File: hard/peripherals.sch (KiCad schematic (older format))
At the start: 12 parts, among them J3 PJ-3062-CO, U1 ADXL362BCCZ-RLX, U2 ADXL345BCCZ-RL7

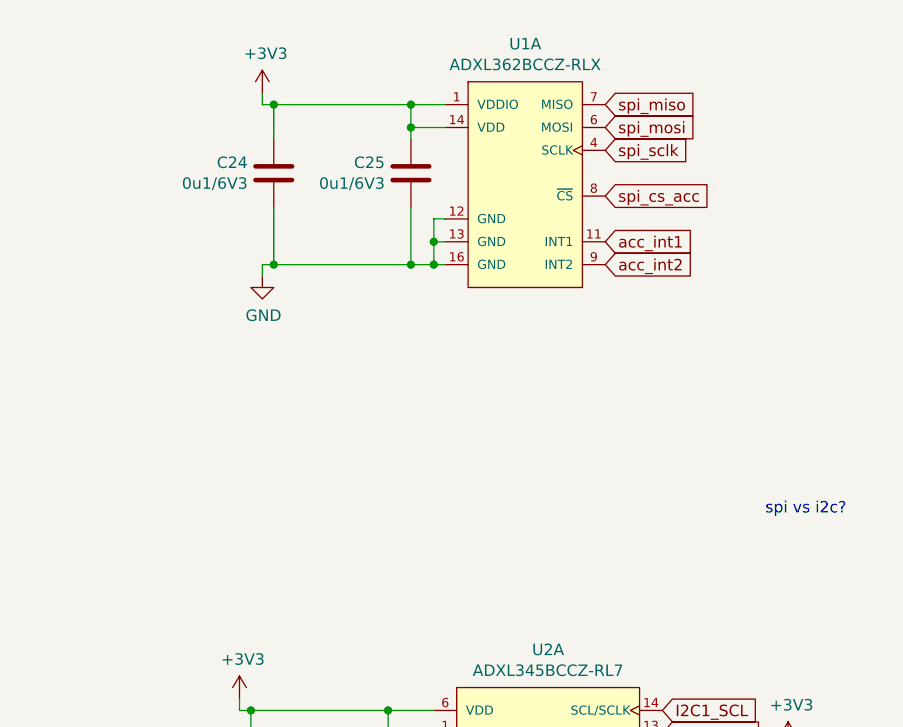
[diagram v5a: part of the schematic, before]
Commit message: general layout update
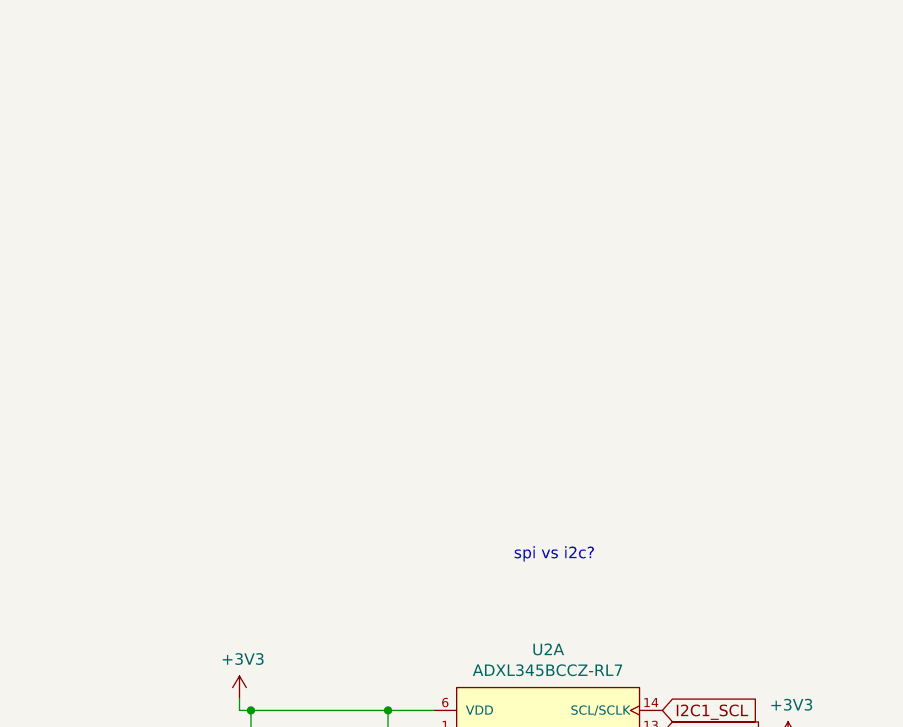
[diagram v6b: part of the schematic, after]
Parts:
- removed C24, C25: 0u1/6V3, Capacitor_SMD:C_0402_1005Metric, symbol Device:C
- removed U1: ADXL362BCCZ-RLX, led_matrix:Sensors_AnalogDevices_ADXL362BCCZ-RX, symbol led_matrix:ADXL362BCCZ-RLX
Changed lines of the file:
@@
 $EndDescr
-$Comp
-L Device:C C25
-U 1 1 613EB9FD
-P 8300 2150
-F 0 "C25" H 8186 2104 50  0000 R CNN
-F 1 "0u1/6V3" H 8186 2195 50  0000 R CNN
-F 2 "Capacitor_SMD:C_0402_1005Metric" H 8338 2000 50  0001 C CNN
-F 3 "~" H 8300 2150 50  0001 C CNN
-	1    8300 2150
-	1    0    0    1
-$EndComp
-$Comp
-L Device:C C24
-U 1 1 613EE98F
-P 7700 2150
-F 0 "C24" H 7586 2104 50  0000 R CNN
-F 1 "0u1/6V3" H 7586 2195 50  0000 R CNN
-F 2 "Capacitor_SMD:C_0402_1005Metric" H 7738 2000 50  0001 C CNN
-F 3 "~" H 7700 2150 50  0001 C CNN
-	1    7700 2150
-	1    0    0    1
-$EndComp
-$Comp
-L power:+3V3 #PWR0200
-U 1 1 613EF1A2
-P 7650 1800
-F 0 "#PWR0200" H 7650 1650 50  0001 C CNN
-F 1 "+3V3" H 7665 1973 50  0000 C CNN
-F 2 "" H 7650 1800 50  0001 C CNN
-F 3 "" H 7650 1800 50  0001 C CNN
-	1    7650 1800
-	1    0    0    -1
-$EndComp
-$Comp
-L power:GND #PWR0201
-U 1 1 613F21F8
-P 7650 2600
-F 0 "#PWR0201" H 7650 2350 50  0001 C CNN
-F 1 "GND" H 7655 2427 50  0000 C CNN
-F 2 "" H 7650 2600 50  0001 C CNN
-F 3 "" H 7650 2600 50  0001 C CNN
-	1    7650 2600
-	1    0    0    -1
-$EndComp
-Wire Wire Line
-	8450 2550 8400 2550
-Wire Wire Line
-	7650 2550 7650 2600
-Wire Wire Line
-	7700 2300 7700 2550
-Connection ~ 7700 2550
-Wire Wire Line
-	7700 2550 7650 2550
-Wire Wire Line
-	8300 2300 8300 2550
-Connection ~ 8300 2550
-Wire Wire Line
-	8300 2550 7700 2550
-Wire Wire Line
-	8400 2550 8400 2450
-Wire Wire Line
-	8400 2450 8450 2450
-Connection ~ 8400 2550
-Wire Wire Line
-	8400 2550 8300 2550
-Wire Wire Line
-	8400 2450 8400 2350
-Wire Wire Line
-	8400 2350 8450 2350
-Connection ~ 8400 2450
-Wire Wire Line
-	8450 1950 8300 1950
-Wire Wire Line
-	8300 1950 8300 2000
-Wire Wire Line
-	7650 1800 7650 1850
-Wire Wire Line
-	7650 1850 7700 1850
-Connection ~ 7700 1850
-Text GLabel 9150 1850 2    50   Input ~ 0
-spi_miso
-Text GLabel 9150 1950 2    50   Input ~ 0
-spi_mosi
-Text GLabel 9150 2050 2    50   Input ~ 0
-spi_sclk
-Text GLabel 9150 2250 2    50   Input ~ 0
-spi_cs_acc
-Text GLabel 9150 2450 2    50   Input ~ 0
-acc_int1
-Text GLabel 9150 2550 2    50   Input ~ 0
-acc_int2
-Wire Wire Line
-	7700 1850 7700 2000
-Wire Wire Line
-	8300 1850 7700 1850
-Wire Wire Line
-	8450 1850 8300 1850
-Connection ~ 8300 1850
-Connection ~ 8300 1950
-Wire Wire Line
-	8300 1950 8300 1850
 $Comp
 L led_matrix:ADXL345BCCZ-RL7 U2
@@
 F 8 "ACCEL 2-16G I2C/SPI 14LGA" H 8900 4400 50  0001 C CNN "Description"
 	1    8900 4400
-	1    0    0    -1
-$EndComp
-$Comp
-L led_matrix:ADXL362BCCZ-RLX U1
-U 1 1 61433069
-P 8800 1750
-F 0 "U1" H 8800 1915 50  0000 C CNN
-F 1 "ADXL362BCCZ-RLX" H 8800 1824 50  0000 C CNN
-F 2 "led_matrix:Sensors_AnalogDevices_ADXL362BCCZ-RX" H 8800 1750 50  0001 C CNN
-F 3 "https://www.analog.com/media/en/technical-documentation/data-sheets/ADXL362.pdf" H 8800 2250 50  0001 C CNN
-F 4 "ADXL362BCCZ-RL7CT-ND" H 8700 1750 50  0001 C CNN "DigiKey_Part_Number"
-F 5 "C59641" H 8800 1750 50  0001 C CNN "JLCPCB_Part_Number"
-F 6 "Analog Devices" H 8700 1750 50  0001 C CNN "MF"
-F 7 "ADXL362BCCZ-RL" H 8700 1750 50  0001 C CNN "MPN"
-F 8 "ACCELEROMETER 2-8G SPI 16LGA" H 8700 1750 50  0001 C CNN "Description"
-	1    8800 1750
 	1    0    0    -1
 $EndComp
@@
 Text GLabel 9400 5100 2    50   Input ~ 0
 acc_int2
-Text Notes 9850 3650 0    50   ~ 0
+Text Notes 8750 3850 0    50   ~ 0
 spi vs i2c?
 $Comp

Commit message: layout process
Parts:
- added C25, C28: 0u1/6V3, Capacitor_SMD:C_0402_1005Metric, symbol Device:C
- added U1: DNP, led_matrix:Sensors_AnalogDevices_ADXL362BCCZ-RX, symbol led_matrix:ADXL362BCCZ-RLX
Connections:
- net +3V3: now also C25.2, C28.2, U1.1 (VDDIO), U1.14 (VDD); no longer U2.7 (~CS~)
- net GND: now also C25.1, C28.1, U1.12 (GND), U1.13 (GND), U1.16 (GND); no longer U2.12 (SDO/ALT_ADDRESS)
- net I2C1_SCL renamed SPI2_SCLK
- net SPI2_SCLK: now also U1.4 (SCLK)
- net I2C1_SDA renamed SPI2_MOSI
- net SPI2_MOSI: now also U1.6 (MOSI)
- net acc_int1 renamed ACC_INT1
- net ACC_INT1: now also U1.11 (INT1)
- net acc_int2 renamed ACC_INT2
- net ACC_INT2: now also U1.9 (INT2)
- new net SPI2_CS_ACC: U1.8 (~CS~), U2.7 (~CS~)
- new net SPI2_MISO: U1.7 (MISO), U2.12 (SDO/ALT_ADDRESS)
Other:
- moved on the sheet: C26, C27, D1026, D1027, D1028, J3, R206, R207, U2A

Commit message: release candidate. ready for review by @lukekaese
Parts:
- added D?: LTST-S270TBKT, led_matrix:LED_LiteOn_LTST-S270TBKT, symbol led_matrix:LTST-S270TBKT
- added M?: 2N7002,215, Package_TO_SOT_SMD:SOT-23, symbol led_matrix:2N7002,215
- added R?: 3K3, Resistor_SMD:R_0402_1005Metric, symbol Device:R
- added R?: 1K8, Resistor_SMD:R_0402_1005Metric, symbol Device:R
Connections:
- net GND: now also M?.2 (S)
- new net: D?.A, R?.1
- new net: D?.C, M?.3 (D)
- new net: M?.1 (G), R?.1
- new net +5V: R?.2
- new net LED_STATUS: R?.2
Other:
- note added: "Accelerometer\n(populate only one)"
- note added: "Analog In"
- note added: "Status LED"
- note removed: "Sensory & Analog Signals"
- note removed: "spi vs i2c?"
- moved on the sheet: C25, C26, C27, C28, D1026, D1027, D1028, J3, R206, R207, U1A, U2A
